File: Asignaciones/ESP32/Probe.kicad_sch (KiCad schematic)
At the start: 36 parts, among them J2 USB_B_Micro, J4 Conn_01x17, J5 Conn_01x17, Q1 2SC4213, Q2 2SC4213, U1 esp32-devkitM-1, U2 CP2102N-Axx-xQFN28, U4 LM1117MP-3.3

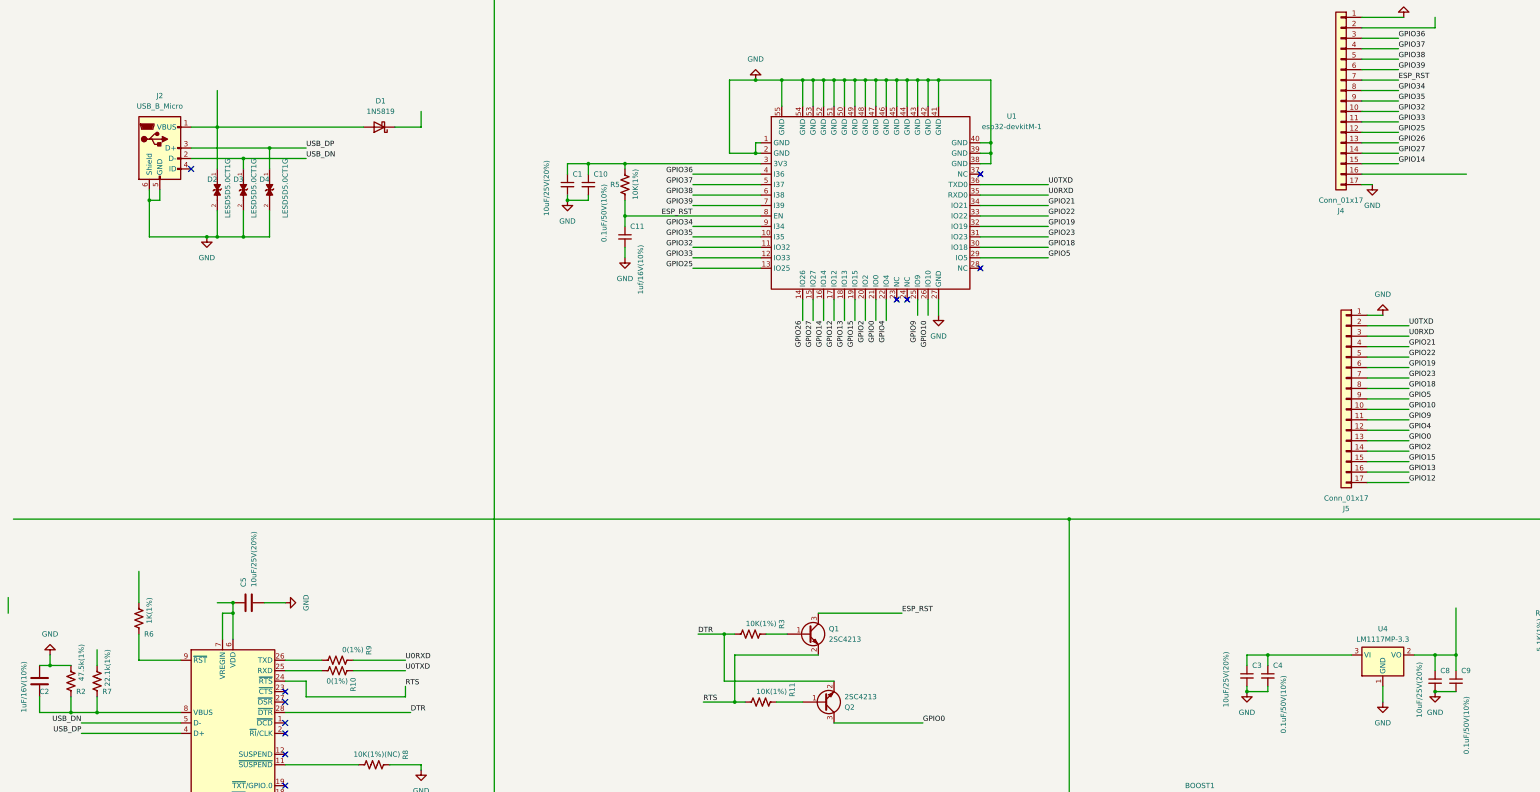
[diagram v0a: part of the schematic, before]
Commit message: Nuevas asignaciones y cambios
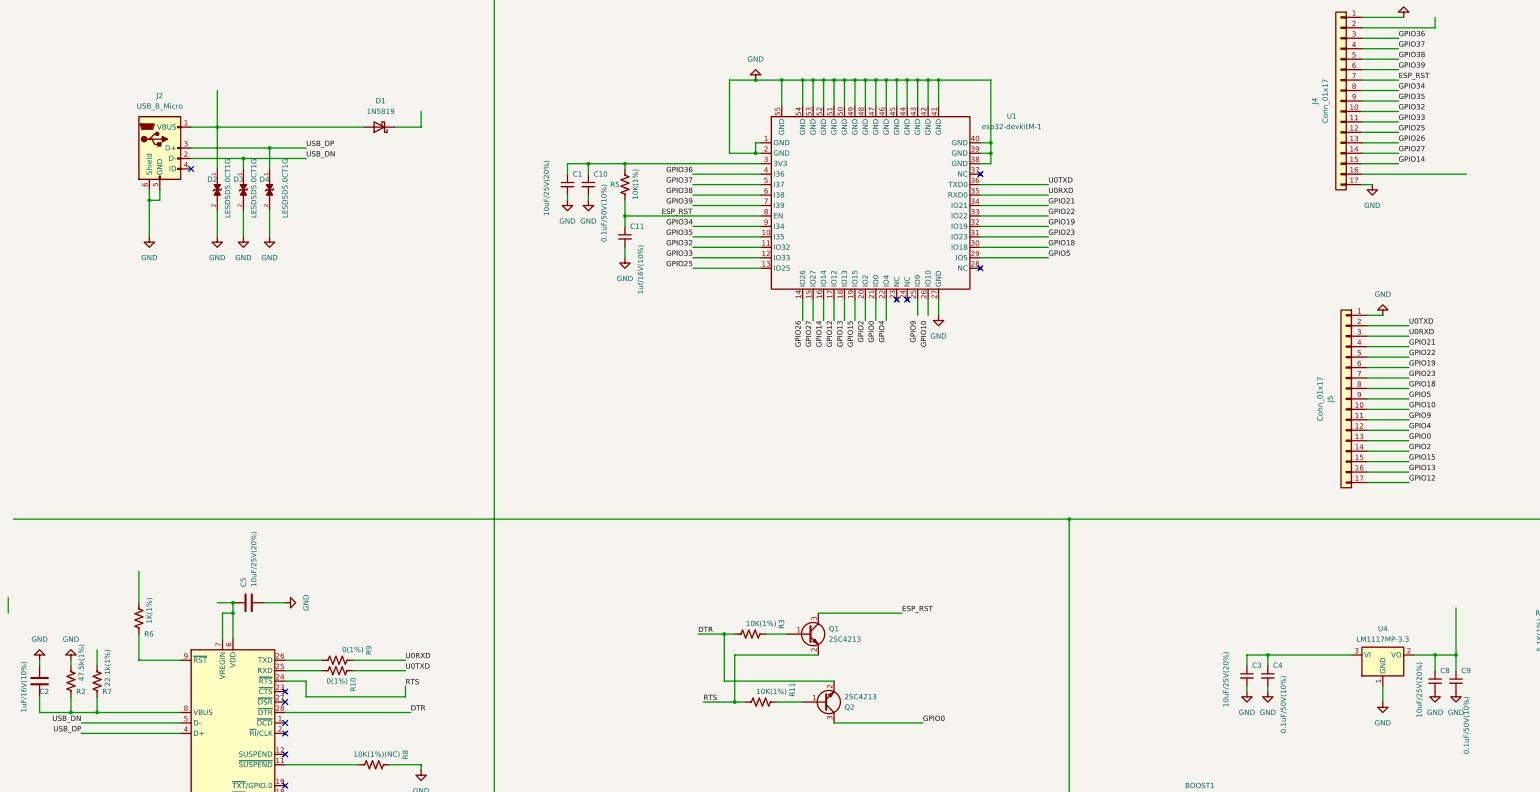
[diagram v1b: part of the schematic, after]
